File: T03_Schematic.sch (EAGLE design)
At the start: 25 parts, among them U1 ATMEGA328P-MU

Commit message: rev 2 of schematic
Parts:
- removed G1: SL-340/SM3.6V, battery:SL-340/SM3.6V
- removed R8: (no value), adafruit:R-US_M0805
- removed U1: ATMEGA328P-MU, Ava:ATMEGA328P-MU
- added BAT1: (no value), SparkFun-Electromechanical:BATTERYAAA
- added HEADER: AVR_SPI_PRG_6PTH, SparkFun-Connectors:AVR_SPI_PRG_6PTH
- added U2: ATMEGA328P_PDIP, SparkFun-DigitalIC:ATMEGA328P_PDIP
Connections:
- removed net XTAL2: BY1.1, CRYSTAL.1, U1.PB7
- new net N$11: HEADER.3, U2.PB5(SCK)
- new net N$12: HEADER.5, U2.PC6(/RESET)
- new net N$13: BY1.1, CRYSTAL.1, U2.PB7(XTAL2/TOSC2)
- new net N$7: HEADER.4, U2.PB3(MOSI/OC2)
- new net N$8: HEADER.6, U2.GND@1, U2.GND@2
- new net N$9: HEADER.1, U2.PB4(MISO)
- net CATH1: now also U2.PD3(INT1); no longer U1.PD0
- net CATH2: now also U2.PD4(XCK/T0); no longer U1.PD1
- net CATH3: now also U2.PD5(T1); no longer U1.PD2
- net CATH4: no longer U1.PB3
- net CONTROL: now also U2.PC0(ADC0); no longer U1.PB4
- net GND: now also BAT1.-; no longer G1.+, R8.1, U1.ADC6, U1.ADC7, U1.AREF, U1.GND
- net GREN1: now also U2.PD6(AIN0); no longer U1.PD3
- net GREN2: now also U2.PD7(AIN1); no longer U1.PD4
- net GREN3: now also U2.PB0(ICP); no longer U1.PD5
- net PLAY1: no longer U1.PB1
- net PLAY2: no longer U1.PB2
- net RED1: now also U2.PD0(RXD); no longer U1.PD6
- net RED2: now also U2.PD1(TXD); no longer U1.PD7
- net RED3: now also U2.PD2(INT0); no longer U1.PB0
- net SELECT: now also U2.PB1(OC1A); no longer R8.2, U1.PB5
- net VCC: now also BAT1.+, HEADER.2, U2.AVCC, U2.VCC; no longer G1.-, U1.AVCC, U1.VCC, U1.VCC_2
- net XTAL1: now also U2.PB6(XTAL1/TOSC1); no longer U1.PB6
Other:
- note added: "2"
- note added: "Tic Tac Toe Game with LEDs"
- moved on the sheet: BY1, BY2, BYCAP, CRYSTAL, LD1, LD10, LD2, LD3, LD4, LD5, LD6, LD7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

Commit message: rev 3
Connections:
- removed net N$7: HEADER.4, U2.PB3(MOSI/OC2)
- removed net N$9: HEADER.1, U2.PB4(MISO)
- net CATH4: now also HEADER.4, U2.PB3(MOSI/OC2)
- net PLAY1: now also U2.PB2(SS/OC1B)
- net PLAY2: now also HEADER.1, U2.PB4(MISO)
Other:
- note added: "3"
- note added: "Revision 3 is complete and ERC-error free We just need to add values to the components and figure out what to do with AREF"
- note removed: "2"
- moved on the sheet: HEADER, LD1, LD10, LD2, LD3, LD4, LD5, LD6, LD7, LD8, LD9, R1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

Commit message: rev 4
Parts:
- added BYCAP1: (no value), adafruit:C-USC0805
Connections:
- net GND: now also BYCAP1.2
- net VCC: now also BYCAP1.1
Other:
- note added: "4"
- note removed: "3"
- note removed: "Revision 3 is complete and ERC-error free We just need to add values to the components and figure out what to do with AREF"
- moved on the sheet: BYCAP
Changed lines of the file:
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@@
 <part name="P+4" library="supply1" deviceset="VCC" device=""/>
 <part name="P+5" library="supply1" deviceset="VCC" device=""/>
+<part name="BYCAP1" library="adafruit" deviceset="C-US" device="C0805"/>
+<part name="SUPPLY2" library="supply2" deviceset="GND" device=""/>
+<part name="SUPPLY5" library="supply2" deviceset="GND" device=""/>
+<part name="P+6" library="supply1" deviceset="VCC" device=""/>
 </parts>
 <sheets>
@@
 <plain>
 <text x="180.34" y="30.48" size="1.778" layer="91">Tic Tac Toe Game with LEDs</text>
-<text x="269.24" y="7.62" size="2.54" layer="92">3</text>
-<text x="10.16" y="200.66" size="2.1844" layer="91">Revision 3 is complete and ERC-error free
-We just need to add values to the components and figure out what to do with AREF</text>
+<text x="269.24" y="7.62" size="2.54" layer="92">4</text>
 </plain>
 <instances>
@@
 <instance part="R5" gate="G$1" x="236.22" y="50.8" rot="R90"/>
 <instance part="R6" gate="G$1" x="137.16" y="48.26"/>
-<instance part="BYCAP" gate="G$1" x="76.2" y="20.32"/>
+<instance part="BYCAP" gate="G$1" x="10.16" y="152.4"/>
 <instance part="POT" gate="G$1" x="246.38" y="66.04" rot="R270"/>
 <instance part="SELECT_BUTTON" gate="G$1" x="121.92" y="50.8" rot="R270"/>
@@
 <instance part="P+4" gate="VCC" x="226.06" y="48.26"/>
 <instance part="P+5" gate="VCC" x="83.82" y="91.44"/>
+<instance part="BYCAP1" gate="G$1" x="27.94" y="152.4"/>
+<instance part="SUPPLY2" gate="GND" x="27.94" y="144.78"/>
+<instance part="SUPPLY5" gate="GND" x="10.16" y="144.78"/>
+<instance part="P+6" gate="VCC" x="10.16" y="165.1"/>
 </instances>
 <busses>
@@
 <wire x1="96.52" y1="30.48" x2="104.14" y2="30.48" width="0.1524" layer="91"/>
 <wire x1="104.14" y1="30.48" x2="104.14" y2="15.24" width="0.1524" layer="91"/>
+</segment>
+<segment>
+<pinref part="BYCAP1" gate="G$1" pin="2"/>
+<pinref part="SUPPLY2" gate="GND" pin="GND"/>
+</segment>
+<segment>
 <pinref part="BYCAP" gate="G$1" pin="2"/>
-<wire x1="76.2" y1="15.24" x2="104.14" y2="15.24" width="0.1524" layer="91"/>
-<junction x="104.14" y="15.24"/>
+<pinref part="SUPPLY5" gate="GND" pin="GND"/>
 </segment>
 </net>
@@
 </segment>
 <segment>
-<pinref part="U2" gate="G$1" pin="AVCC"/>
 <pinref part="U2" gate="G$1" pin="VCC"/>
-<wire x1="43.18" y1="162.56" x2="43.18" y2="160.02" width="0.1524" layer="91"/>
-<junction x="43.18" y="160.02"/>
-<wire x1="43.18" y1="160.02" x2="30.48" y2="160.02" width="0.1524" layer="91"/>
+<wire x1="43.18" y1="160.02" x2="35.56" y2="160.02" width="0.1524" layer="91"/>
 <pinref part="P+1" gate="VCC" pin="VCC"/>
+<wire x1="35.56" y1="160.02" x2="30.48" y2="160.02" width="0.1524" layer="91"/>
+<wire x1="35.56" y1="160.02" x2="35.56" y2="157.48" width="0.1524" layer="91"/>
+<junction x="35.56" y="160.02"/>
+<pinref part="BYCAP1" gate="G$1" pin="1"/>
+<wire x1="35.56" y1="157.48" x2="27.94" y2="157.48" width="0.1524" layer="91"/>
+<wire x1="27.94" y1="157.48" x2="27.94" y2="154.94" width="0.1524" layer="91"/>
 </segment>
 <segment>
 <pinref part="BAT1" gate="G$1" pin="+"/>
-<pinref part="BYCAP" gate="G$1" pin="1"/>
-<wire x1="86.36" y1="30.48" x2="76.2" y2="30.48" width="0.1524" layer="91"/>
-<wire x1="76.2" y1="30.48" x2="76.2" y2="22.86" width="0.1524" layer="91"/>
-<wire x1="76.2" y1="30.48" x2="68.58" y2="30.48" width="0.1524" layer="91"/>
-<junction x="76.2" y="30.48"/>
+<wire x1="86.36" y1="30.48" x2="68.58" y2="30.48" width="0.1524" layer="91"/>
 <pinref part="P+2" gate="VCC" pin="VCC"/>
 <wire x1="68.58" y1="30.48" x2="68.58" y2="35.56" width="0.1524" layer="91"/>
@@
 <pinref part="P+5" gate="VCC" pin="VCC"/>
 <wire x1="76.2" y1="88.9" x2="83.82" y2="88.9" width="0.1524" layer="91"/>
+</segment>
+<segment>
+<pinref part="U2" gate="G$1" pin="AVCC"/>
+<wire x1="43.18" y1="162.56" x2="10.16" y2="162.56" width="0.1524" layer="91"/>
+<pinref part="BYCAP" gate="G$1" pin="1"/>
+<wire x1="10.16" y1="162.56" x2="10.16" y2="154.94" width="0.1524" layer="91"/>
+<pinref part="P+6" gate="VCC" pin="VCC"/>
+<junction x="10.16" y="162.56"/>
 </segment>
 </net>
@@
 </schematic>
 </drawing>
-<compatibility>
-<note version="6.3" minversion="6.2.2" severity="warning">
-Since Version 6.2.2 text objects can contain more than one line,
-which will not be processed correctly with this version.
-</note>
-</compatibility>
 </eagle>

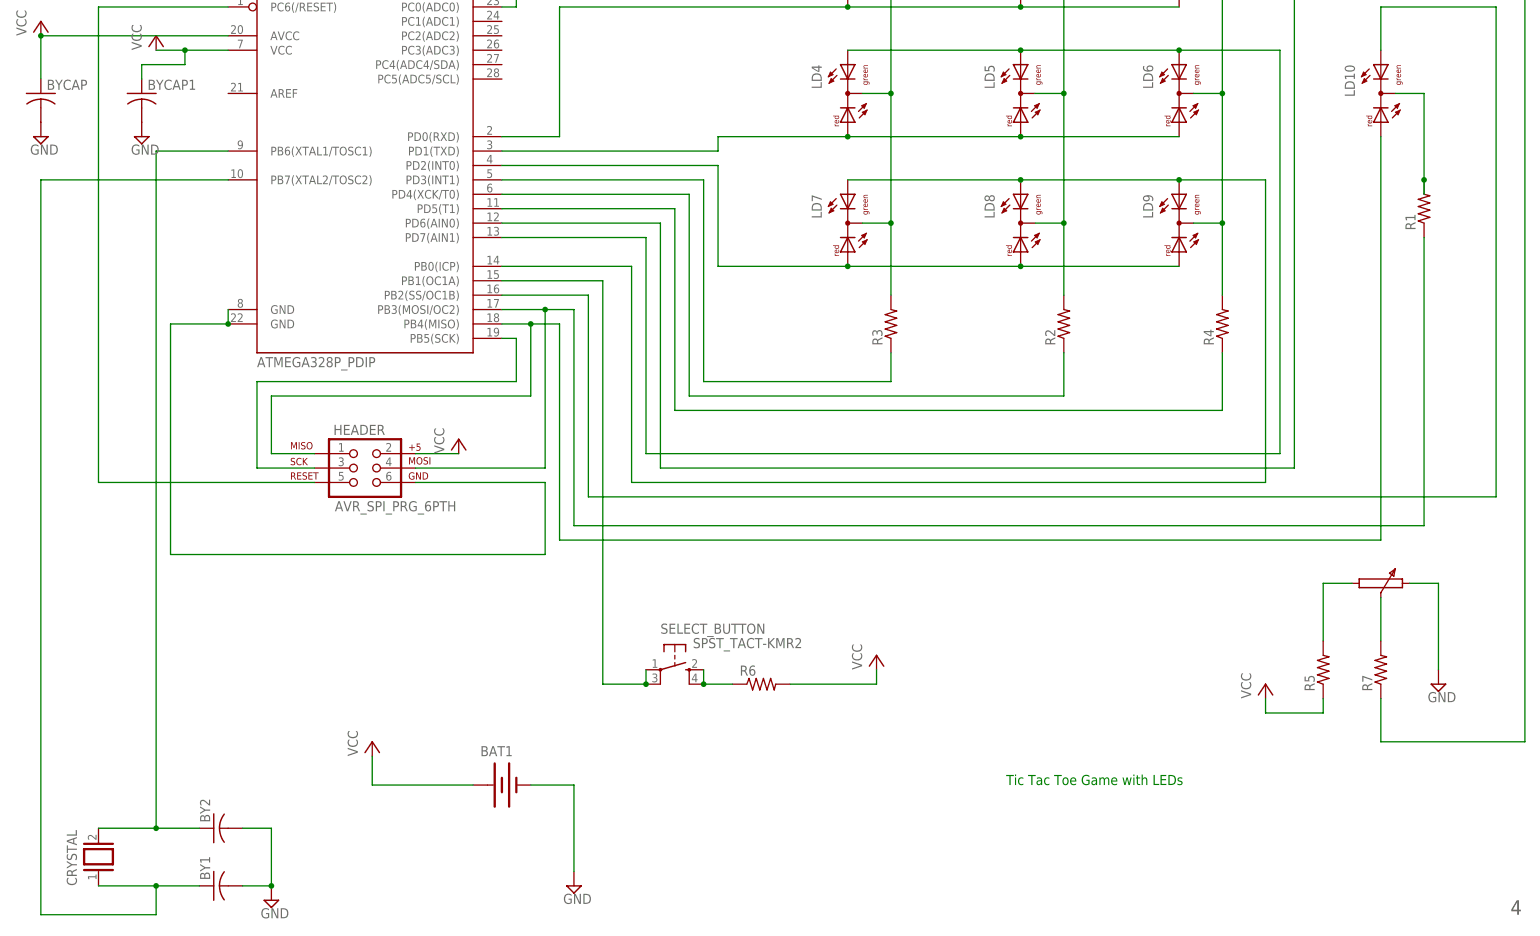
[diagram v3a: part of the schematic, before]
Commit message: Added values to components
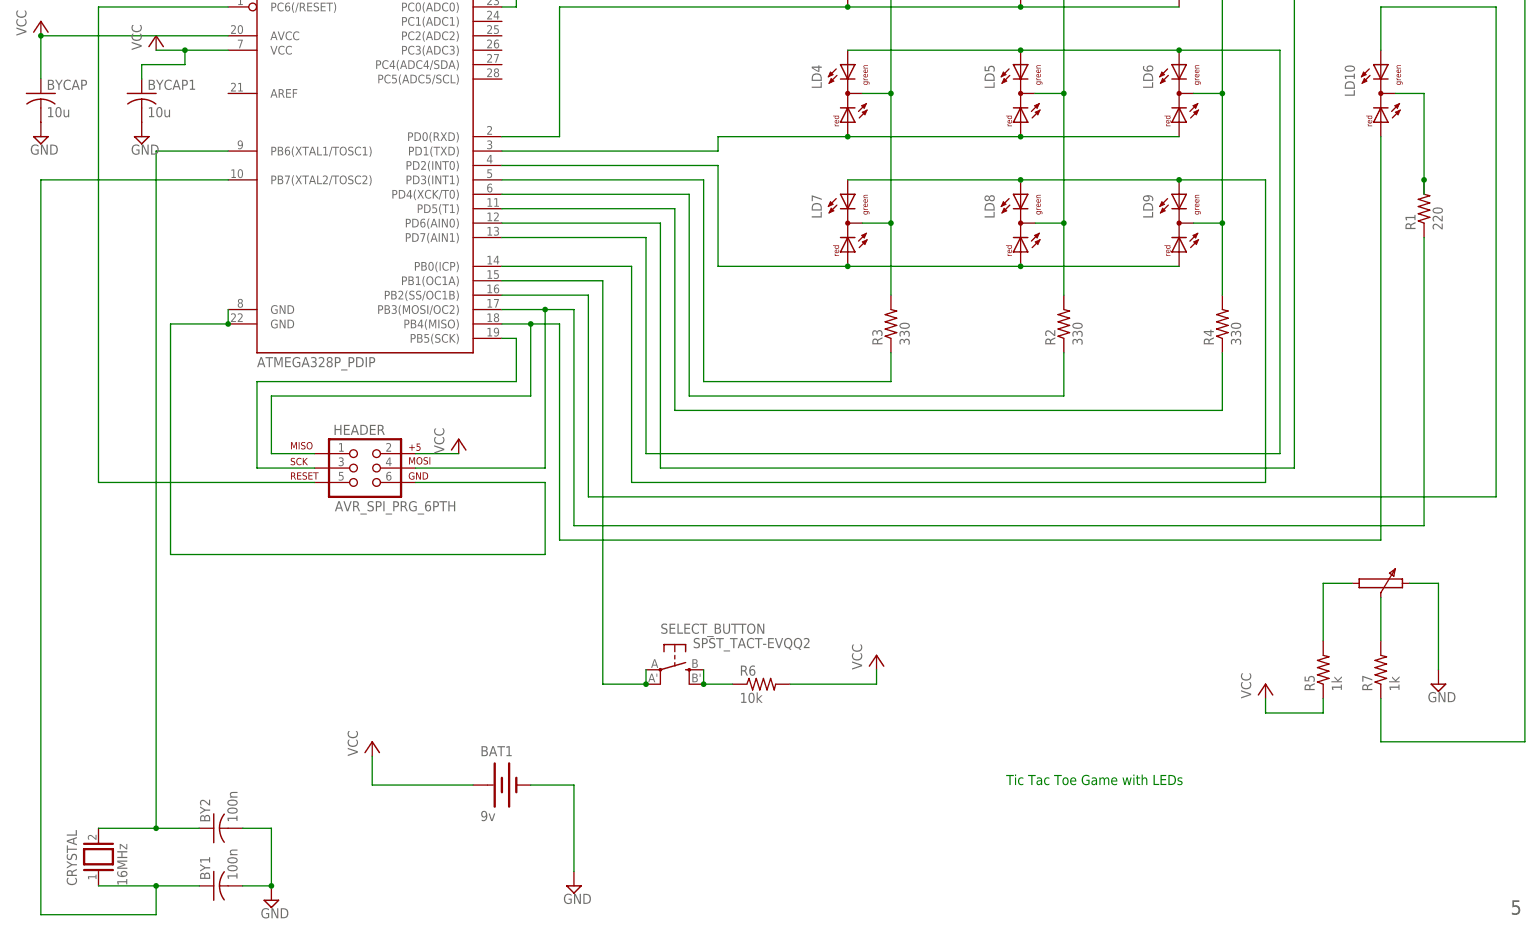
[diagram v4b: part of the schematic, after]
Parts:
- BAT1: value (none) -> 9v; device SparkFun-Electromechanical:BATTERYAAA -> SparkFun-Electromechanical:BATTERY9V
- BY1, BY2: value (none) -> 100n
- BYCAP, BYCAP1: value (none) -> 10u
- CRYSTAL: value (none) -> 16MHz
- R1: value (none) -> 220
- R2, R3, R4: value (none) -> 330
- R5, R7: value (none) -> 1k
- R6: value (none) -> 10k
- SELECT_BUTTON: value SPST_TACT-KMR2 -> SPST_TACT-EVQQ2; device adafruit:SPST_TACT-KMR2 -> adafruit:SPST_TACT-EVQQ2
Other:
- note added: "5"
- note removed: "4"
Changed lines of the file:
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@@
 <grid distance="0.1" unitdist="inch" unit="inch" style="lines" multiple="1" display="no" altdistance="0.01" altunitdist="inch" altunit="inch"/>
 <layers>
-<layer number="1" name="Top" color="4" fill="1" visible="no" active="no"/>
-<layer number="16" name="Bottom" color="1" fill="1" visible="no" active="no"/>
-<layer number="17" name="Pads" color="2" fill="1" visible="no" active="no"/>
-<layer number="18" name="Vias" color="2" fill="1" visible="no" active="no"/>
-<layer number="19" name="Unrouted" color="6" fill="1" visible="no" active="no"/>
-<layer number="20" name="Dimension" color="15" fill="1" visible="no" active="no"/>
-<layer number="21" name="tPlace" color="7" fill="1" visible="no" active="no"/>
-<layer number="22" name="bPlace" color="7" fill="1" visible="no" active="no"/>
-<layer number="23" name="tOrigins" color="15" fill="1" visible="no" active="no"/>
-<layer number="24" name="bOrigins" color="15" fill="1" visible="no" active="no"/>
-<layer number="25" name="tNames" color="7" fill="1" visible="no" active="no"/>
-<layer number="26" name="bNames" color="7" fill="1" visible="no" active="no"/>
-<layer number="27" name="tValues" color="7" fill="1" visible="no" active="no"/>
-<layer number="28" name="bValues" color="7" fill="1" visible="no" active="no"/>
+<layer number="1" name="Top" color="4" fill="1" visible="yes" active="no"/>
+<layer number="16" name="Bottom" color="1" fill="1" visible="yes" active="no"/>
+<layer number="17" name="Pads" color="2" fill="1" visible="yes" active="no"/>
+<layer number="18" name="Vias" color="2" fill="1" visible="yes" active="no"/>
+<layer number="19" name="Unrouted" color="6" fill="1" visible="yes" active="no"/>
+<layer number="20" name="Dimension" color="15" fill="1" visible="yes" active="no"/>
+<layer number="21" name="tPlace" color="7" fill="1" visible="yes" active="no"/>
+<layer number="22" name="bPlace" color="7" fill="1" visible="yes" active="no"/>
+<layer number="23" name="tOrigins" color="15" fill="1" visible="yes" active="no"/>
+<layer number="24" name="bOrigins" color="15" fill="1" visible="yes" active="no"/>
+<layer number="25" name="tNames" color="7" fill="1" visible="yes" active="no"/>
+<layer number="26" name="bNames" color="7" fill="1" visible="yes" active="no"/>
+<layer number="27" name="tValues" color="7" fill="1" visible="yes" active="no"/>
+<layer number="28" name="bValues" color="7" fill="1" visible="yes" active="no"/>
 <layer number="29" name="tStop" color="7" fill="3" visible="no" active="no"/>
 <layer number="30" name="bStop" color="7" fill="6" visible="no" active="no"/>
@@
 <layer number="35" name="tGlue" color="7" fill="4" visible="no" active="no"/>
 <layer number="36" name="bGlue" color="7" fill="5" visible="no" active="no"/>
-<layer number="37" name="tTest" color="7" fill="1" visible="no" active="no"/>
-<layer number="38" name="bTest" color="7" fill="1" visible="no" active="no"/>
+<layer number="37" name="tTest" color="7" fill="1" visible="yes" active="no"/>
+<layer number="38" name="bTest" color="7" fill="1" visible="yes" active="no"/>
 <layer number="39" name="tKeepout" color="4" fill="11" visible="no" active="no"/>
 <layer number="40" name="bKeepout" color="1" fill="11" visible="no" active="no"/>
@@
 <layer number="44" name="Drills" color="7" fill="1" visible="no" active="no"/>
 <layer number="45" name="Holes" color="7" fill="1" visible="no" active="no"/>
-<layer number="46" name="Milling" color="3" fill="1" visible="no" active="no"/>
-<layer number="47" name="Measures" color="7" fill="1" visible="no" active="no"/>
-<layer number="48" name="Document" color="7" fill="1" visible="no" active="no"/>
-<layer number="49" name="Reference" color="7" fill="1" visible="no" active="no"/>
-<layer number="50" name="dxf" color="7" fill="1" visible="no" active="no"/>
-<layer number="51" name="tDocu" color="7" fill="1" visible="no" active="no"/>
-<layer number="52" name="bDocu" color="7" fill="1" visible="no" active="no"/>
-<layer number="53" name="tGND_GNDA" color="7" fill="9" visible="no" active="no"/>
-<layer number="54" name="bGND_GNDA" color="1" fill="9" visible="no" active="no"/>
-<layer number="56" name="wert" color="7" fill="1" visible="no" active="no"/>
-<layer number="57" name="tCAD" color="7" fill="1" visible="no" active="no"/>
+<layer number="46" name="Milling" color="3" fill="1" visible="yes" active="no"/>
+<layer number="47" name="Measures" color="7" fill="1" visible="yes" active="no"/>
+<layer number="48" name="Document" color="7" fill="1" visible="yes" active="no"/>
+<layer number="49" name="Reference" color="7" fill="1" visible="yes" active="no"/>
+<layer number="50" name="dxf" color="7" fill="1" visible="yes" active="no"/>
+<layer number="51" name="tDocu" color="7" fill="1" visible="yes" active="no"/>
+<layer number="52" name="bDocu" color="7" fill="1" visible="yes" active="no"/>
+<layer number="53" name="tGND_GNDA" color="7" fill="9" visible="yes" active="no"/>
+<layer number="54" name="bGND_GNDA" color="1" fill="9" visible="yes" active="no"/>
+<layer number="56" name="wert" color="7" fill="1" visible="yes" active="no"/>
+<layer number="57" name="tCAD" color="7" fill="1" visible="yes" active="no"/>
 <layer number="90" name="Modules" color="5" fill="1" visible="yes" active="yes"/>
 <layer number="91" name="Nets" color="2" fill="1" visible="yes" active="yes"/>
@@
 </classes>
 <parts>
-<part name="R1" library="adafruit" deviceset="R-US_" device="M0805"/>
-<part name="R2" library="adafruit" deviceset="R-US_" device="M0805"/>
-<part name="R3" library="adafruit" deviceset="R-US_" device="M0805"/>
-<part name="R4" library="adafruit" deviceset="R-US_" device="M0805"/>
-<part name="R5" library="adafruit" deviceset="R-US_" device="M0805"/>
-<part name="R6" library="adafruit" deviceset="R-US_" device="M0805"/>
-<part name="BYCAP" library="adafruit" deviceset="C-US" device="C0805"/>
+<part name="R1" library="adafruit" deviceset="R-US_" device="M0805" value="220"/>
+<part name="R2" library="adafruit" deviceset="R-US_" device="M0805" value="330"/>
+<part name="R3" library="adafruit" deviceset="R-US_" device="M0805" value="330"/>
+<part name="R4" library="adafruit" deviceset="R-US_" device="M0805" value="330"/>
+<part name="R5" library="adafruit" deviceset="R-US_" device="M0805" value="1k"/>
+<part name="R6" library="adafruit" deviceset="R-US_" device="M0805" value="10k"/>
+<part name="BYCAP" library="adafruit" deviceset="C-US" device="C0805" value="10u"/>
 <part name="POT" library="docu-dummy" deviceset="POT" device=""/>
-<part name="SELECT_BUTTON" library="adafruit" deviceset="SPST_TACT" device="-KMR2"/>
+<part name="SELECT_BUTTON" library="adafruit" deviceset="SPST_TACT" device="-EVQQ2" value="SPST_TACT-EVQQ2"/>
 <part name="SUPPLY1" library="supply2" deviceset="GND" device=""/>
-<part name="CRYSTAL" library="special" deviceset="XTAL/S" device=""/>
+<part name="CRYSTAL" library="special" deviceset="XTAL/S" device="" value="16MHz"/>
 <part name="LD1" library="led" deviceset="DUOLED-RG-C" device=""/>
 <part name="LD2" library="led" deviceset="DUOLED-RG-C" device=""/>
@@
 <part name="LD9" library="led" deviceset="DUOLED-RG-C" device=""/>
 <part name="LD10" library="led" deviceset="DUOLED-RG-C" device=""/>
-<part name="R7" library="adafruit" deviceset="R-US_" device="M0805"/>
+<part name="R7" library="adafruit" deviceset="R-US_" device="M0805" value="1k"/>
 <part name="SUPPLY3" library="supply2" deviceset="GND" device=""/>
-<part name="BY1" library="adafruit" deviceset="C-US" device="C0805"/>
-<part name="BY2" library="adafruit" deviceset="C-US" device="C0805"/>
+<part name="BY1" library="adafruit" deviceset="C-US" device="C0805" value="100n"/>
+<part name="BY2" library="adafruit" deviceset="C-US" device="C0805" value="100n"/>
 <part name="SUPPLY4" library="supply2" deviceset="GND" device=""/>
 <part name="U2" library="SparkFun-DigitalIC" deviceset="ATMEGA328P_PDIP" device=""/>
 <part name="FRAME1" library="frames" deviceset="FRAME_A_L" device=""/>
-<part name="BAT1" library="SparkFun-Electromechanical" deviceset="BATTERY" device="AAA"/>
+<part name="BAT1" library="SparkFun-Electromechanical" deviceset="BATTERY" device="9V" value="9v"/>
 <part name="HEADER" library="SparkFun-Connectors" deviceset="AVR_SPI_PRG_6" device="PTH"/>
 <part name="P+1" library="supply1" deviceset="VCC" device=""/>
@@
 <part name="P+4" library="supply1" deviceset="VCC" device=""/>
 <part name="P+5" library="supply1" deviceset="VCC" device=""/>
-<part name="BYCAP1" library="adafruit" deviceset="C-US" device="C0805"/>
+<part name="BYCAP1" library="adafruit" deviceset="C-US" device="C0805" value="10u"/>
 <part name="SUPPLY2" library="supply2" deviceset="GND" device=""/>
 <part name="SUPPLY5" library="supply2" deviceset="GND" device=""/>
@@
 <plain>
 <text x="180.34" y="30.48" size="1.778" layer="91">Tic Tac Toe Game with LEDs</text>
-<text x="269.24" y="7.62" size="2.54" layer="92">4</text>
+<text x="269.24" y="7.62" size="2.54" layer="92">5</text>
 </plain>
 <instances>
